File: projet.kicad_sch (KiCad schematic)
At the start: 1 part, among them J1 CONN_C2000_2x24

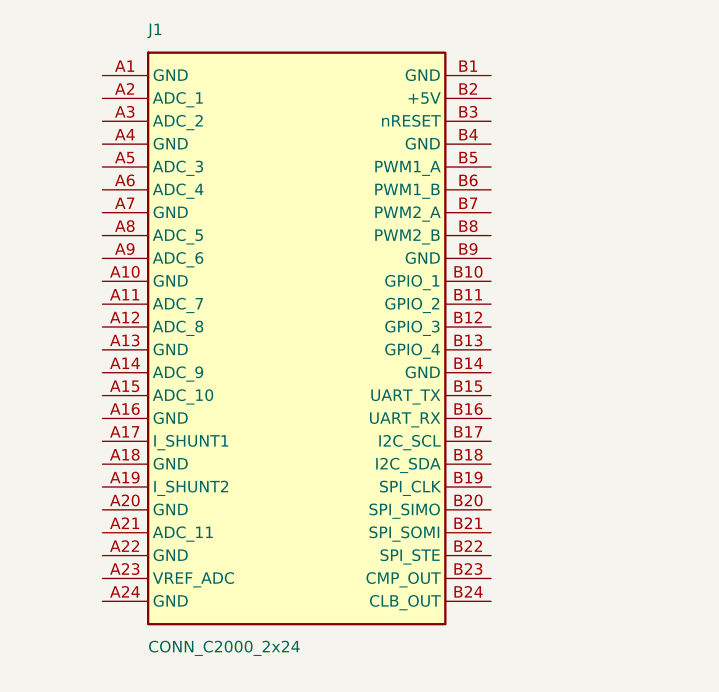
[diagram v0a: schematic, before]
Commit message: Cable les 14 GND et le +5V du connecteur, avec PWR_FLAG sur chaque net
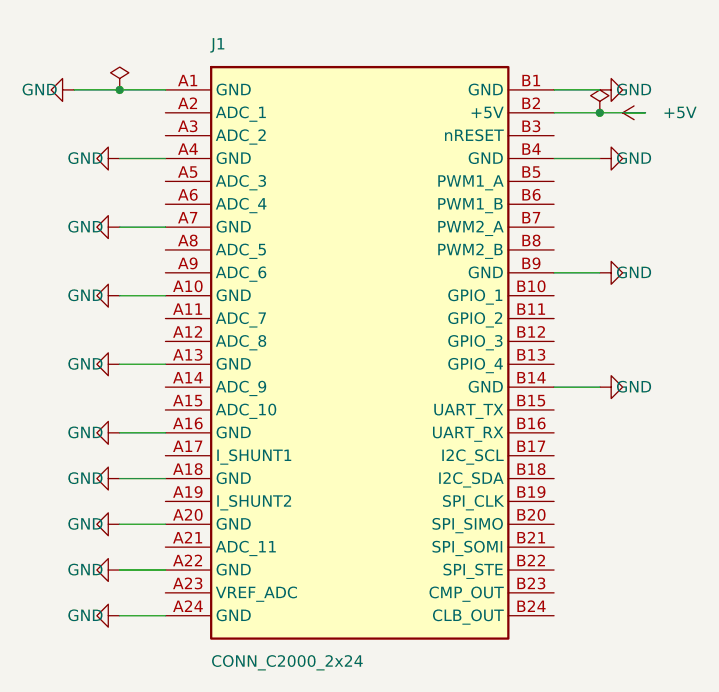
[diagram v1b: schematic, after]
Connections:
- net GND: now reaches J1.A1 (GND)
- net GND: now also J1.A10 (GND), J1.A13 (GND), J1.A16 (GND), J1.A18 (GND), J1.A20 (GND), J1.A22 (GND), J1.A24 (GND), J1.A4 (GND), J1.A7 (GND), J1.B1 (GND), J1.B14 (GND), J1.B4 (GND), J1.B9 (GND)
- net +5V: now reaches J1.B2 (+5V)
